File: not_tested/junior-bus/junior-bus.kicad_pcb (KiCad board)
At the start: 2 copper layers, 81.3 x 99.1 mm, 4 parts, among them J1 C64AB, J2 C64AC, J3 C64AC, J4 C64AC

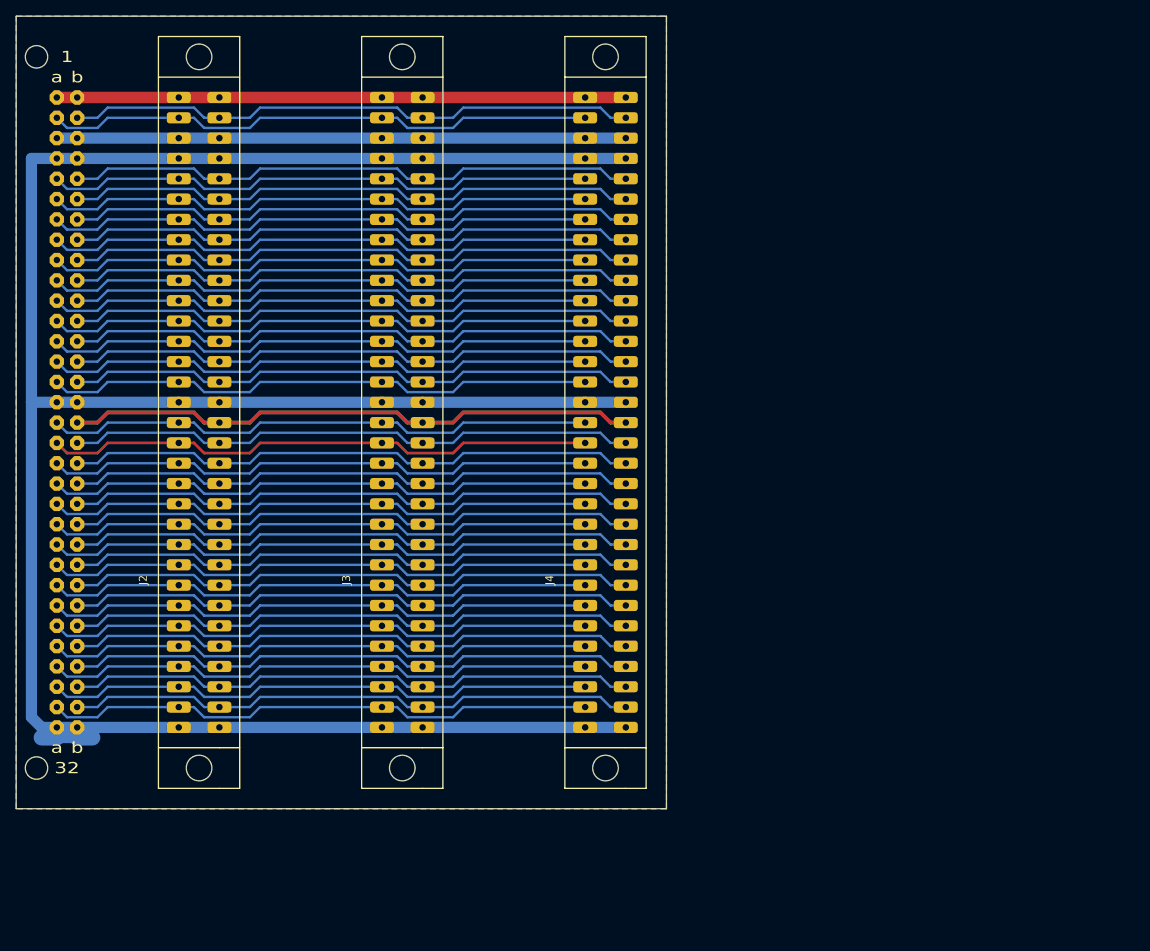
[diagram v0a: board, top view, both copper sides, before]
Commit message: update Junior Bus subproject
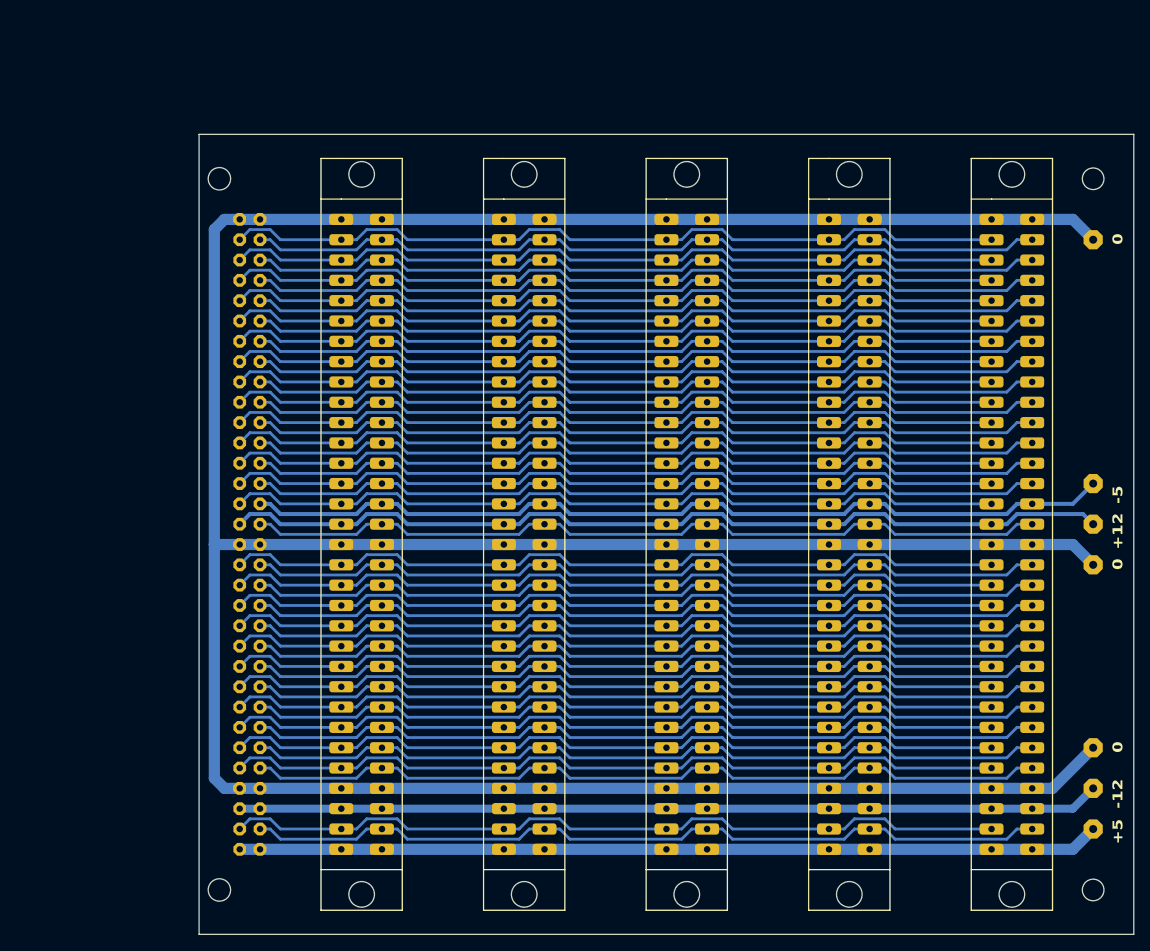
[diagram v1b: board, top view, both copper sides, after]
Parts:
- added J10: Conn_01x01_Pin, elektor:PIN, F.Cu at (182.9, 137.2)
- added J11: Conn_01x01_Pin, elektor:PIN, F.Cu at (182.9, 132.1)
- added J12: Conn_01x01_Pin, elektor:PIN, F.Cu at (182.9, 109.2)
- added J13: Conn_01x01_Pin, elektor:PIN, F.Cu at (182.9, 68.6)
- added J5: C64AC, elektor:DI41612-AC-F, F.Cu at (154.9, 144.8)
- added J6: C64AC, elektor:DI41612-AC-F, F.Cu at (175.3, 144.8)
- added J7: Conn_01x01_Pin, elektor:PIN, F.Cu at (182.9, 142.2)
- added J8: Conn_01x01_Pin, elektor:PIN, F.Cu at (182.9, 99.1)
- added J9: Conn_01x01_Pin, elektor:PIN, F.Cu at (182.9, 104.1)
- added REF1: MountingHole_2.7mm_M2.5_ISO14580, MountingHole:MountingHole_2.7mm_M2.5_ISO14580, F.Cu at (182.9, 61.0)
- added REF2: MountingHole_2.7mm_M2.5_ISO14580, MountingHole:MountingHole_2.7mm_M2.5_ISO14580, F.Cu at (182.9, 149.9)
- J1: footprint elektor:DIN-41612-AB -> elektor:DIN-41612-AB-small-pads; moved to B.Cu
- moved J2 97.4 mm to (94.0, 144.8), turned to 90 degrees
- moved J1 96.7 mm to (78.7, 144.8)
- moved J3 96.2 mm to (114.3, 144.8), turned to 90 degrees
- moved J4 95.2 mm to (134.6, 144.8), turned to 90 degrees
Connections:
- J1 pad A10: /D7 -> /D6
- J1 pad A11: 11A -> 11C
- J1 pad A12: IRQ -> NMI
- J1 pad A13: 13A -> 13C
- J1 pad A14: 14A -> SO
- J1 pad A15: 15A -> C15
- J1 pad A17: 17A -> +12V
- J1 pad A18: -5V -> 18C
- J1 pad A19: /A15 -> /A14
- J1 pad A2: 2A -> 2C
- J1 pad A20: /A13 -> /A12
- J1 pad A21: /A11 -> /A10
- J1 pad A22: /A9 -> /A8
- J1 pad A23: /A7 -> /A6
- J1 pad A24: /A5 -> /A4
- J1 pad A25: /A3 -> /A2
- J1 pad A26: /A1 -> /A0
- J1 pad A27: 27A -> 27C
- J1 pad A28: 28A -> 28C
- J1 pad A29: 29A -> RW
- J1 pad A30: PHI1 -> EX
- J1 pad A31: RAM.RW -> 31C
- J1 pad A5: RES -> RDY
- J1 pad A6: 6A -> 6C
- J1 pad A7: /D1 -> /D0
- J1 pad A8: /D3 -> /D2
- J1 pad A9: /D5 -> /D4
- J1 pad B10: /D6 -> /D7
- J1 pad B11: 11C -> 11A
- J1 pad B12: NMI -> IRQ
- J1 pad B13: 13C -> 13A
- J1 pad B14: SO -> 14A
- J1 pad B15: C15 -> 15A
- J1 pad B17: +12V -> 17A
- J1 pad B18: 18C -> -5V
- J1 pad B19: /A14 -> /A15
- J1 pad B2: 2C -> 2A
- J1 pad B20: /A12 -> /A13
- J1 pad B21: /A10 -> /A11
- J1 pad B22: /A8 -> /A9
- J1 pad B23: /A6 -> /A7
- J1 pad B24: /A4 -> /A5
- J1 pad B25: /A2 -> /A3
- J1 pad B26: /A0 -> /A1
- J1 pad B27: 27C -> 27A
- J1 pad B28: 28C -> 28A
- J1 pad B29: RW -> 29A
- J1 pad B30: EX -> PHI1
- J1 pad B31: 31C -> RAM.RW
- J1 pad B5: RDY -> RES
- J1 pad B6: 6C -> 6A
- J1 pad B7: /D0 -> /D1
- J1 pad B8: /D2 -> /D3
- J1 pad B9: /D4 -> /D5
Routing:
- net GND: track 302.2 -> 403.4 mm
- net -12V: track 71.1 -> 107.7 mm
- net +5V: track 142.2 -> 107.7 mm
- net /D3: track 69.2 -> 101.8 mm
- net 29A: track 69.2 -> 101.8 mm
- net 11A: track 69.2 -> 101.8 mm
- net /D5: track 69.2 -> 101.8 mm
- net /D1: track 69.2 -> 101.8 mm
- net 27A: track 69.2 -> 101.8 mm
- net /A3: track 69.2 -> 101.8 mm
- net /A13: track 69.2 -> 101.8 mm
- net /A1: track 69.2 -> 101.8 mm
- net 17A: track 69.2 -> 101.8 mm
- net 15A: track 69.2 -> 101.8 mm
- net 13A: track 69.2 -> 101.8 mm
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- removed copper zone on B.Cu, net GND
- removed copper zone on F.Cu, net GND
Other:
- board size 81.3 x 99.1 mm -> 116.8 x 100 mm
- net class Default removed
- board text added: "+12"
- board text added: "+5"
- board text added: "-12"
- board text added: "-5"
- board text added: "0"
